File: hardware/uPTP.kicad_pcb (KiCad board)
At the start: 2 copper layers, 35 x 50 mm, 41 parts, among them J1 Conn_01x04_Pin, J2 PPS_UFL, J3 PPS_SMA, J4 HC-RJ45-055-7, J5 AUX_PWR, U1 CH32V307WCU6, U2 TMI7301, U3 LMR16030SDDAR, U4 XC6206P332MR-G

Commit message: Done for the day
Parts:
- J1: value Conn_01x04_Pin -> UART_HDR
- moved U4 49.3 mm to (134.0, 93.0)
- moved U3 36.1 mm to (142.0, 93.0), turned to 90 degrees
- moved H2 16.4 mm to (124.0, 126.0)
- moved U1 15.0 mm to (129.0, 109.0)
- moved D7 14.2 mm to (122.5, 114.1)
- moved R10 10.0 mm to (148.0, 134.0)
- moved R8 10.0 mm to (139.0, 134.0)
- moved R9 10.0 mm to (146.0, 134.0)
- moved J2 9.00 mm to (126.0, 88.0)
- moved J3 9.00 mm to (126.0, 82.0)
- moved TR1 8.00 mm to (144.0, 109.0)
- moved C3 7.07 mm to (137.0, 106.0), turned to 180 degrees
- moved C4 7.00 mm to (137.0, 112.0)
- moved C5 6.95 mm to (155.0, 99.0)
- moved D5 6.95 mm to (155.0, 102.0)
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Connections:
- J1 pad 1: unconnected-(J1-Pin_1-Pad1) -> GND
- J1 pad 2: unconnected-(J1-Pin_2-Pad2) -> /UART_TX
- J1 pad 3: unconnected-(J1-Pin_3-Pad3) -> /UART_RX
- J1 pad 4: unconnected-(J1-Pin_4-Pad4) -> +3V3
- J5 pad 1: unconnected-(J5-Pin_1-Pad1) -> GND
- J5 pad 2: unconnected-(J5-Pin_2-Pad2) -> /Power/V_AUX
- U1 pad 0: unconnected-(U1-EP-Pad0) -> GND
- U1 pad 12: unconnected-(U1-VSSA-Pad12) -> GND
- U1 pad 18: Net-(U1-VSS-Pad18) -> GND
- U1 pad 49: Net-(U1-VSS-Pad18) -> GND
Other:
- board size 35 x 50 mm -> 40 x 50 mm
- board text added: "TODO line up to 2.54mm grid"

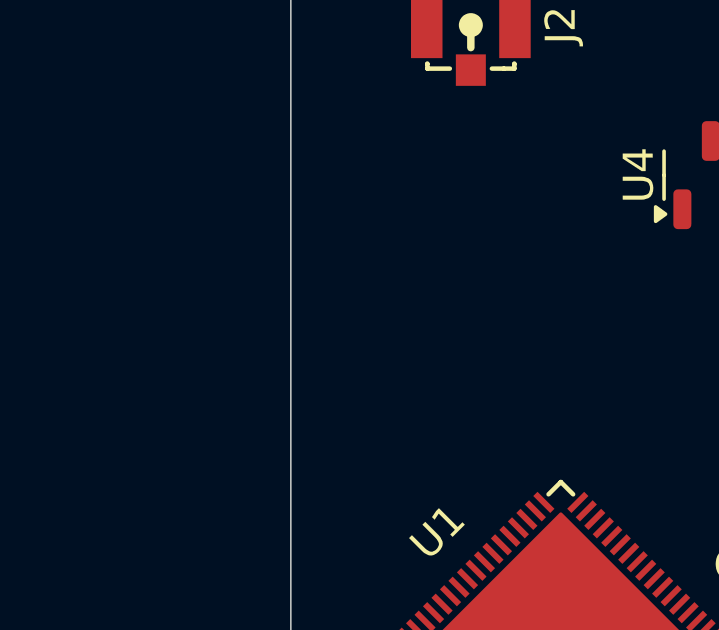
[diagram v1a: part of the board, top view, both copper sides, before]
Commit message: Prep for change to SI3404 https://www.skyworksinc.com/-/media/Skyworks/SL/documents/public/application-notes/an1130-si3404-06x-dg.pdf
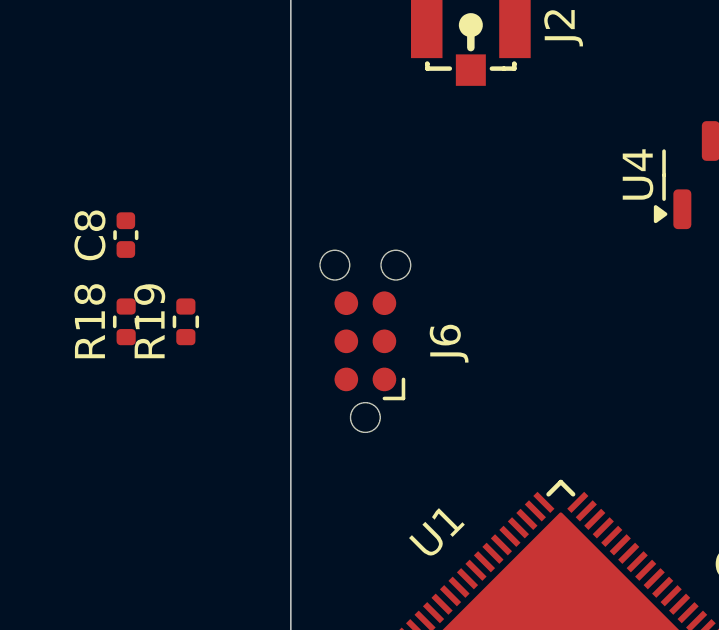
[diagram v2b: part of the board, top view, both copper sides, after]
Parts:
- added C8: 100n, Capacitor_SMD:C_0402_1005Metric, F.Cu at (114.5, 95.0)
- added J6: PROG, Connector:Tag-Connect_TC2030-IDC-NL_2x03_P1.27mm_Vertical, F.Cu at (122.5, 98.5)
- added R18: 10k, Resistor_SMD:R_0402_1005Metric, F.Cu at (114.5, 97.9)
- added R19: 10k, Resistor_SMD:R_0402_1005Metric, F.Cu at (116.5, 97.9)
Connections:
- C6 pad 1: Net-(C6-Pad1) -> /XTAL_OUT
- C7 pad 1: Net-(C7-Pad1) -> /XTAL_IN
- U1 pad 39: unconnected-(U1-PC6-Pad39) -> /ETH_D_RX_P
- U1 pad 40: unconnected-(U1-PC7-Pad40) -> /ETH_D_RX_N
- U1 pad 41: unconnected-(U1-PC8-Pad41) -> /ETH_D_TX_P
- U1 pad 42: unconnected-(U1-PC9-Pad42) -> /ETH_D_TX_N
- U1 pad 46: unconnected-(U1-PA11-Pad46) -> /USB_D_N
- U1 pad 47: unconnected-(U1-PA12-Pad47) -> /USB_D_P
- U1 pad 48: unconnected-(U1-SWDIO-Pad48) -> /SWDIO
- U1 pad 5: unconnected-(U1-OSC_IN-Pad5) -> /XTAL_IN
- U1 pad 52: unconnected-(U1-SWCLK-Pad52) -> /SWCLK
- U1 pad 6: unconnected-(U1-OSC_OUT-Pad6) -> /XTAL_OUT
- U1 pad 63: unconnected-(U1-BOOT0-Pad63) -> Net-(U1-BOOT0)
- U1 pad 7: unconnected-(U1-~{RST}-Pad7) -> /~{RST}

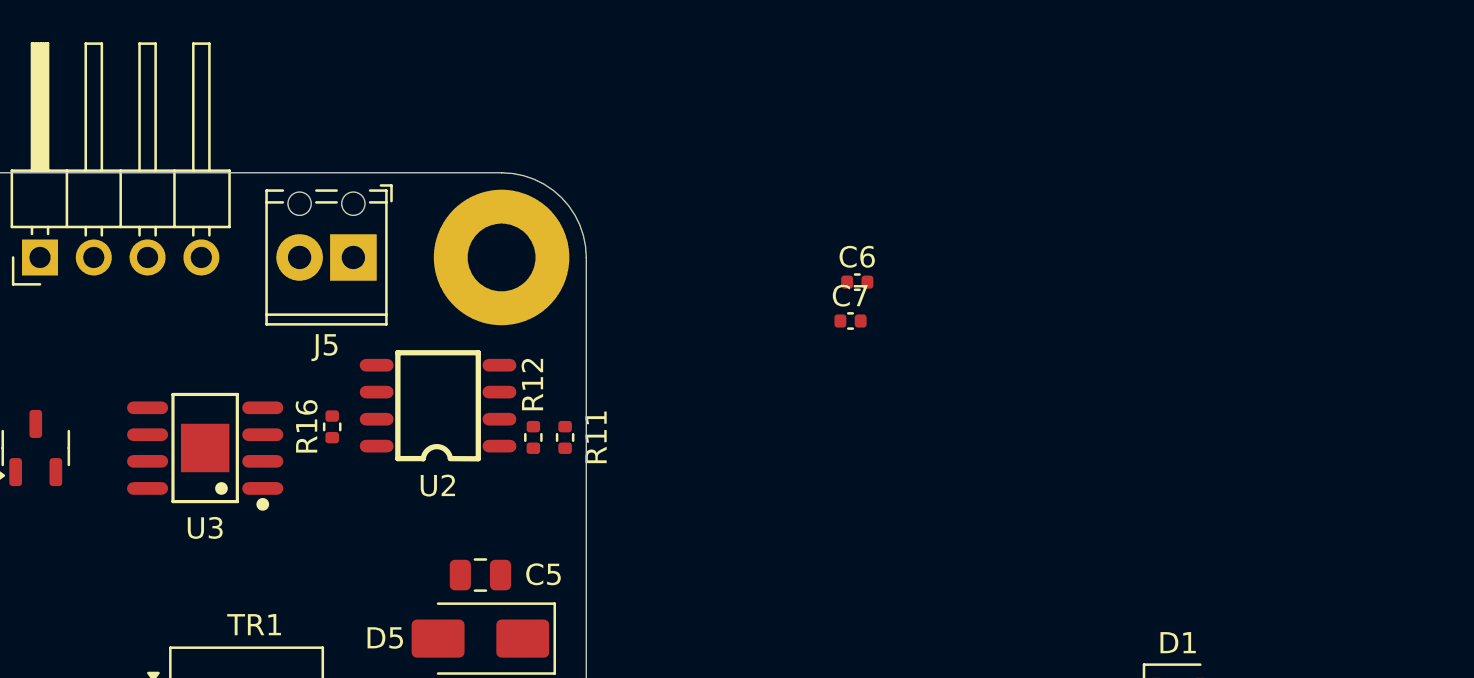
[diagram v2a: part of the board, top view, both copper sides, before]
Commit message: Add SI3404 part
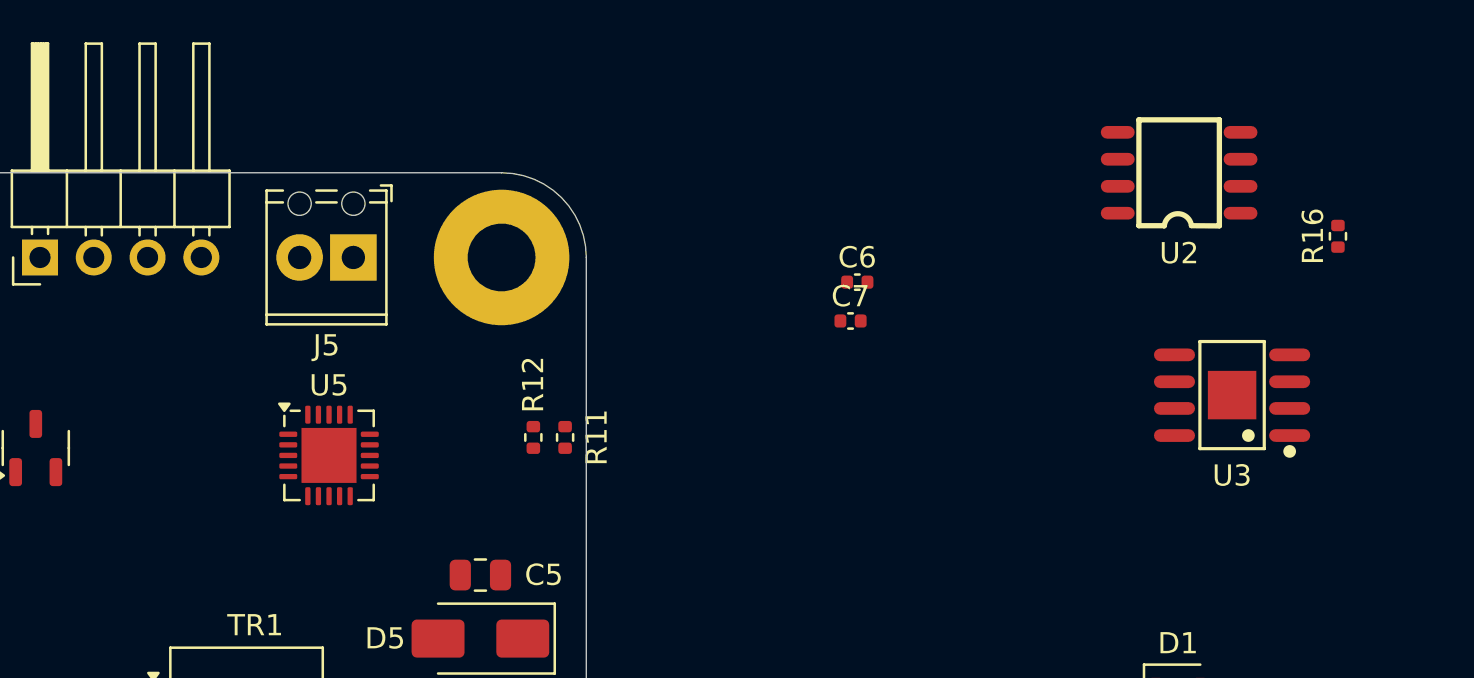
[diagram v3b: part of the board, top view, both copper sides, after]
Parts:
- added U5: SI3404-A-GMR, Package_DFN_QFN:QFN-20-1EP_4x4mm_P0.5mm_EP2.6x2.6mm, F.Cu at (147.8, 93.3)
- moved U3 48.6 mm to (190.5, 90.5)
- moved R16 48.3 mm to (195.5, 83.0)
- moved U2 36.7 mm to (188.0, 80.0)

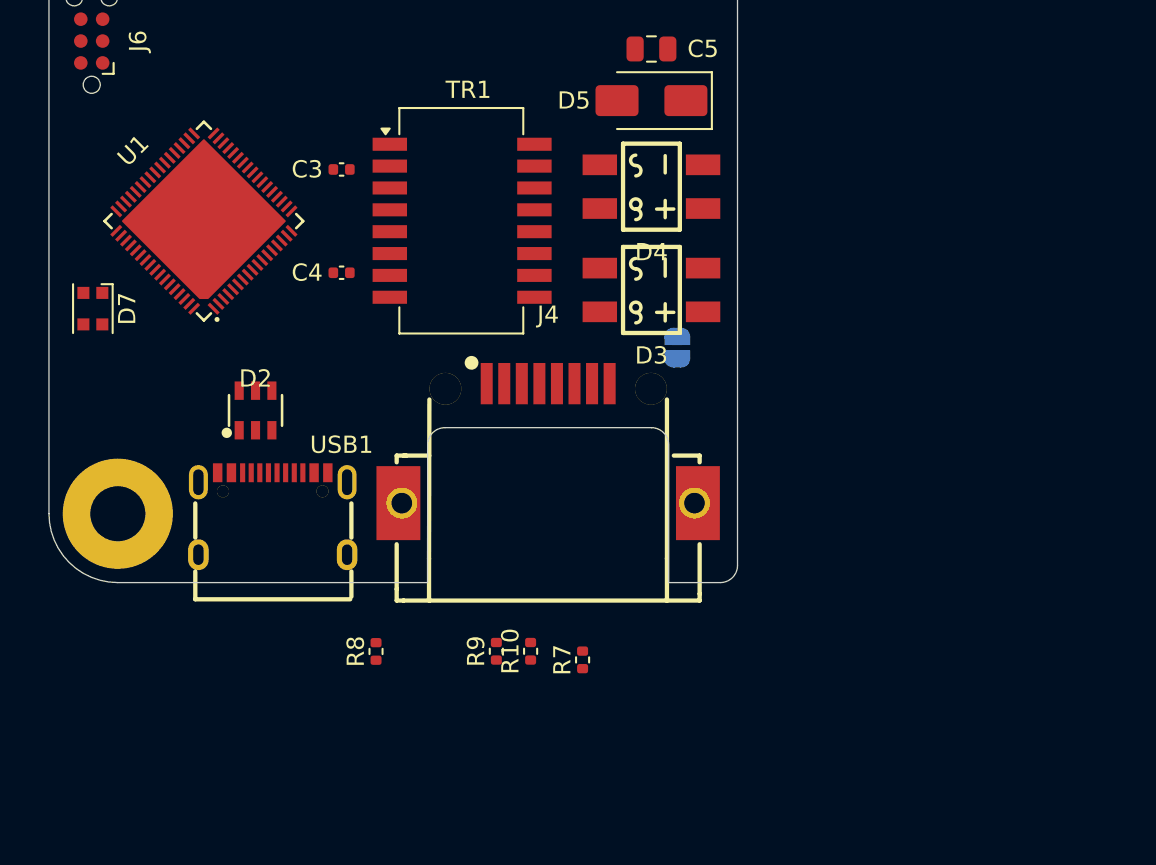
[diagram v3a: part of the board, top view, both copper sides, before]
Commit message: Add XTAL, rough POE Schematic
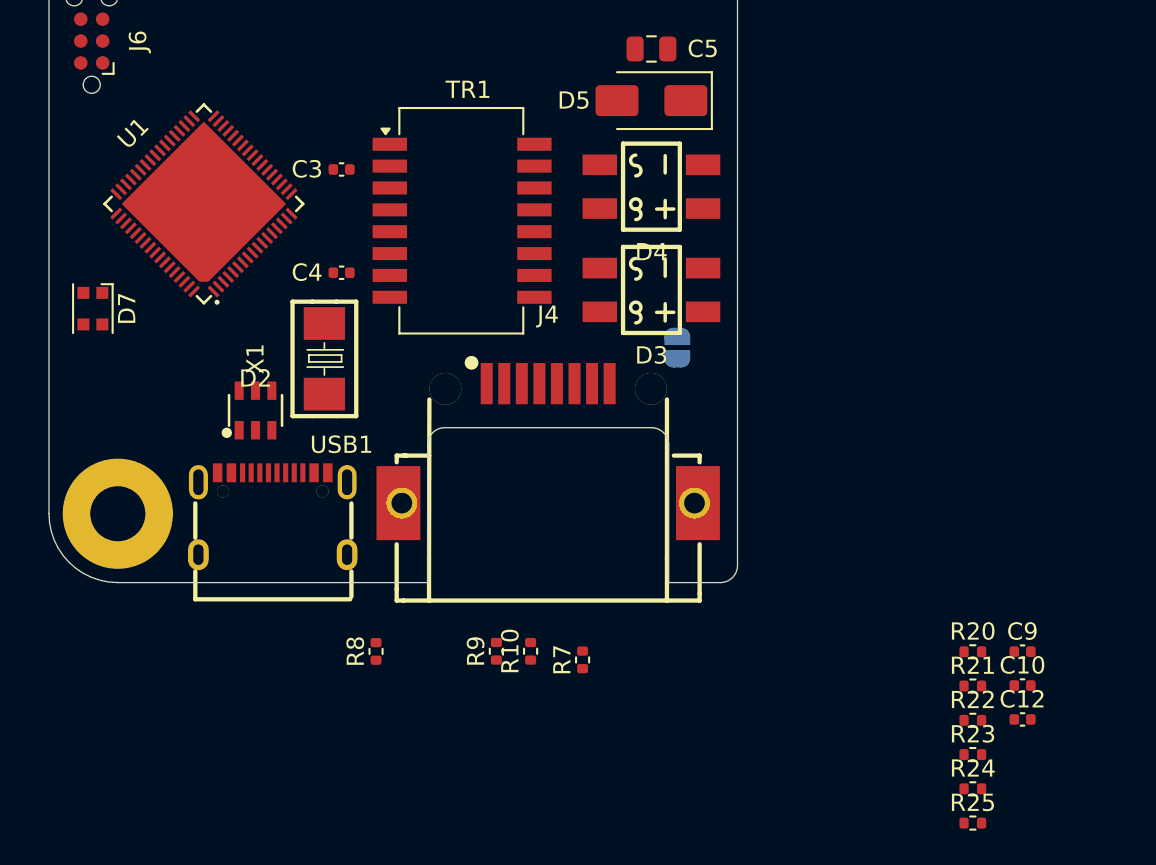
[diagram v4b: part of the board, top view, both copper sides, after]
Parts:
- added C10: 100n, Capacitor_SMD:C_0402_1005Metric, F.Cu at (176.6, 136.0)
- added C12: 100n, Capacitor_SMD:C_0402_1005Metric, F.Cu at (176.6, 137.9)
- added C9: 100n, Capacitor_SMD:C_0402_1005Metric, F.Cu at (176.6, 134.0)
- added R20: 88.7k, Resistor_SMD:R_0402_1005Metric, F.Cu at (173.7, 134.0)
- added R21: 24.3k, Resistor_SMD:R_0402_1005Metric, F.Cu at (173.7, 136.0)
- added R22: 1.2, Resistor_SMD:R_0402_1005Metric, F.Cu at (173.7, 138.0)
- added R23: ?, Resistor_SMD:R_0402_1005Metric, F.Cu at (173.7, 140.0)
- added R24: ?, Resistor_SMD:R_0402_1005Metric, F.Cu at (173.7, 142.0)
- added R25: ?, Resistor_SMD:R_0402_1005Metric, F.Cu at (173.7, 144.0)
- added X1: X50328MSB2GI, uPTP:CRYSTAL-SMD_L5.0-W3.2, F.Cu at (136.0, 117.0)
- C5: value 100n 100V/60V? -> 100n 100V
- R11: value 24.9k -> 24.3k
- R12: value 1k -> 75
- moved U1 1.00 mm to (129.0, 108.0)
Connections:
- C5 pad 1: /Ethernet and POE/ETH_POE_P -> Net-(D5-A1)
- C5 pad 2: /Ethernet and POE/ETH_POE_N -> Net-(D5-A2)
- D5 pad 1: /Ethernet and POE/ETH_POE_P -> Net-(D5-A1)
- D5 pad 2: /Ethernet and POE/ETH_POE_N -> Net-(D5-A2)
- D6 pad 2: /Ethernet and POE/ETH_POE_P -> Net-(D5-A1)
- R11 pad 1: /Ethernet and POE/ETH_POE_P -> Net-(D5-A1)
- R12 pad 2: /Ethernet and POE/ETH_POE_N -> Net-(D5-A2)
- U5 pad 1: unconnected-(U5-ISNS-Pad1) -> Net-(U5-HSO)
- U5 pad 10: unconnected-(U5-RFREQ-Pad10) -> Net-(U5-RFREQ)
- U5 pad 13: unconnected-(U5-VPOS-Pad13) -> Net-(D5-A1)
- U5 pad 14: unconnected-(U5-VNEG-Pad14) -> Net-(D5-A2)
- U5 pad 18: unconnected-(U5-SWO-Pad18) -> Net-(D8-A)
- U5 pad 19: unconnected-(U5-VSS-Pad19) -> /Ethernet and POE/POE_VSS
- U5 pad 2: unconnected-(U5-FBH-Pad2) -> Net-(U5-FBH)
- U5 pad 21: unconnected-(U5-EP-Pad21) -> Net-(D5-A2)
- U5 pad 3: unconnected-(U5-EROUT-Pad3) -> Net-(U5-EROUT)
- U5 pad 4: unconnected-(U5-FBL-Pad4) -> /Ethernet and POE/POE_VSS
- U5 pad 5: unconnected-(U5-VDD-Pad5) -> Net-(U5-VDD)
- U5 pad 6: unconnected-(U5-RDET-Pad6) -> /Ethernet and POE/ETH_POE_DET
- U5 pad 8: unconnected-(U5-HSO-Pad8) -> Net-(U5-HSO)
- U5 pad 9: unconnected-(U5-RCL-Pad9) -> /Ethernet and POE/ETH_POE_CLASS
